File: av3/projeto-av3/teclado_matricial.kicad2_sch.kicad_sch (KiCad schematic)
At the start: 16 parts, among them SW1 SW_Push, SW10 SW_Push, SW11 SW_Push, SW12 SW_Push, SW13 SW_Push, SW14 SW_Push, SW15 SW_Push, SW16 SW_Push, SW2 SW_Push, SW3 SW_Push, SW4 SW_Push, SW5 SW_Push, SW6 SW_Push, SW7 SW_Push, SW8 SW_Push, SW9 SW_Push

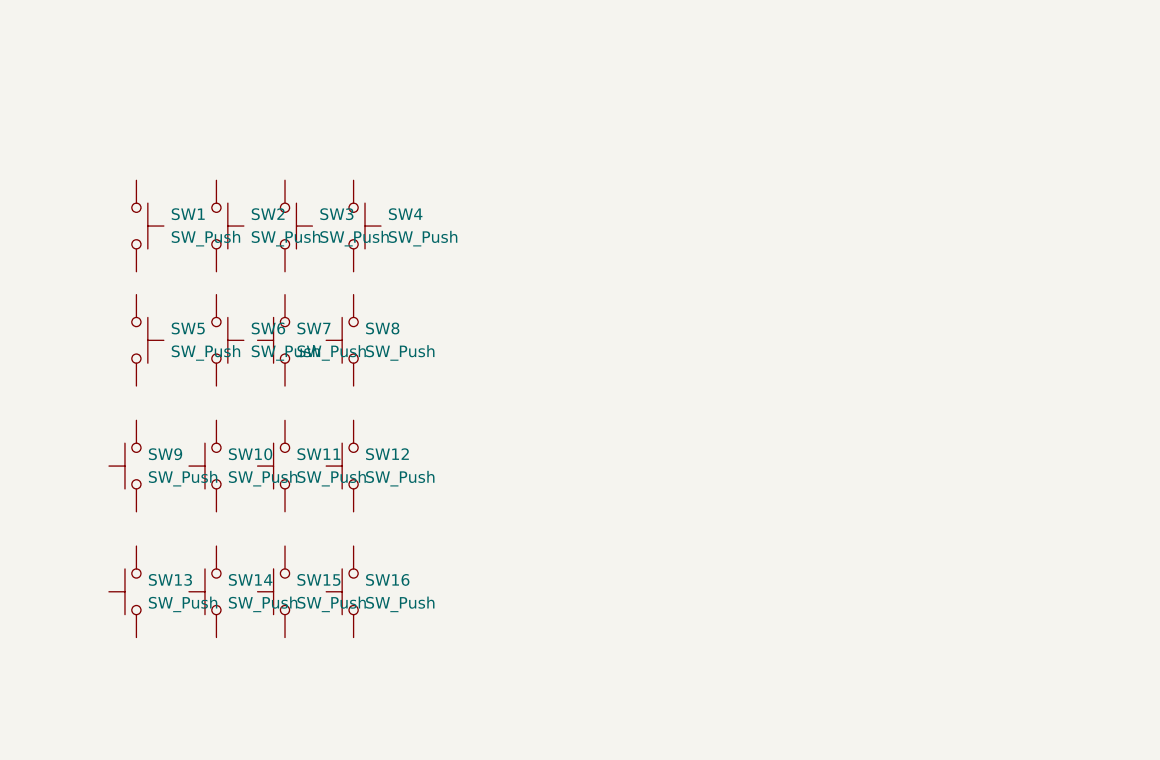
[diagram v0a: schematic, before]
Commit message: Ligação do cristal no atmega2560 e início do esquemático das saídas digitais com relé.
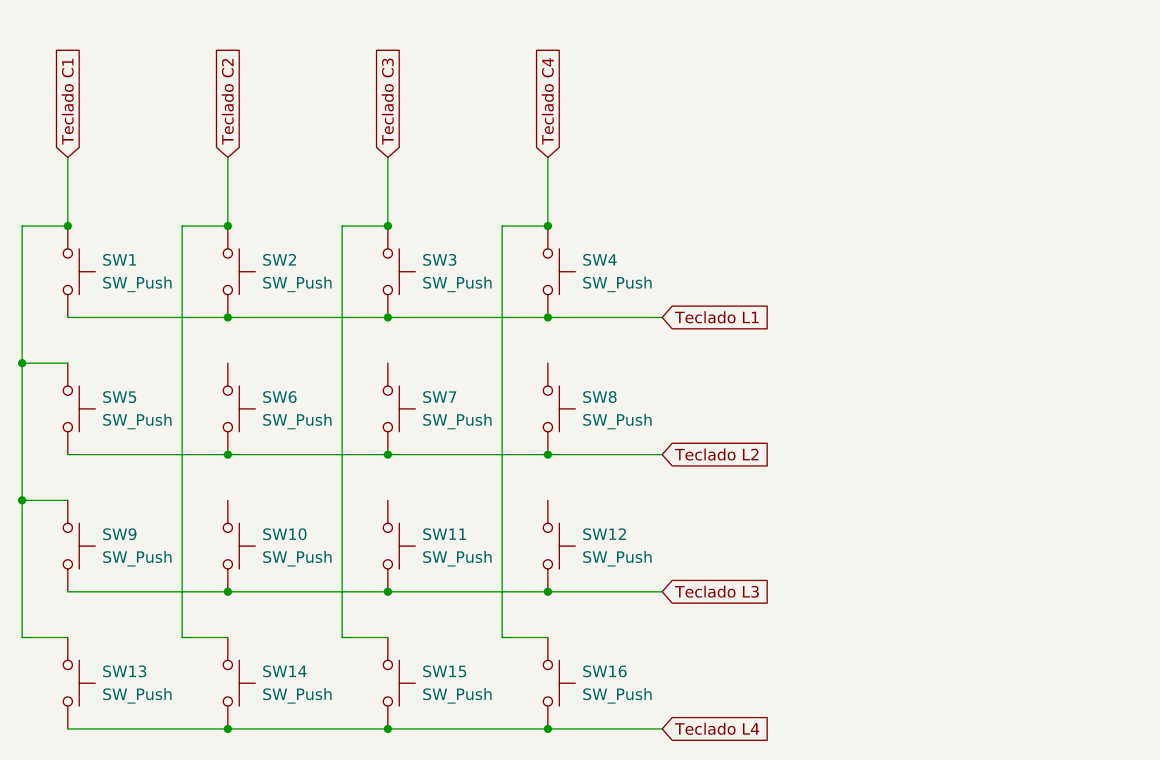
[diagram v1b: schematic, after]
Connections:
- net Teclado L3: now reaches SW10.2
- net Teclado L3: now also SW11.2, SW12.2, SW9.2
- net Teclado L2: now reaches SW7.2
- net Teclado L2: now also SW5.2, SW6.2, SW8.2
- net Teclado C4: now reaches SW16.1
- net Teclado C4: now also SW4.1
- net Teclado L4: now reaches SW16.2
- net Teclado L4: now also SW13.2, SW14.2, SW15.2
- net Teclado L1: now reaches SW4.2
- net Teclado L1: now also SW1.2, SW2.2, SW3.2
- net Teclado C2: now reaches SW2.1
- net Teclado C2: now also SW14.1
- net Teclado C1: now reaches SW1.1
- net Teclado C1: now also SW13.1, SW5.1, SW9.1
- net Teclado C3: now reaches SW15.1
- net Teclado C3: now also SW3.1

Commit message: Maioria dos esquemáticos finalizados.
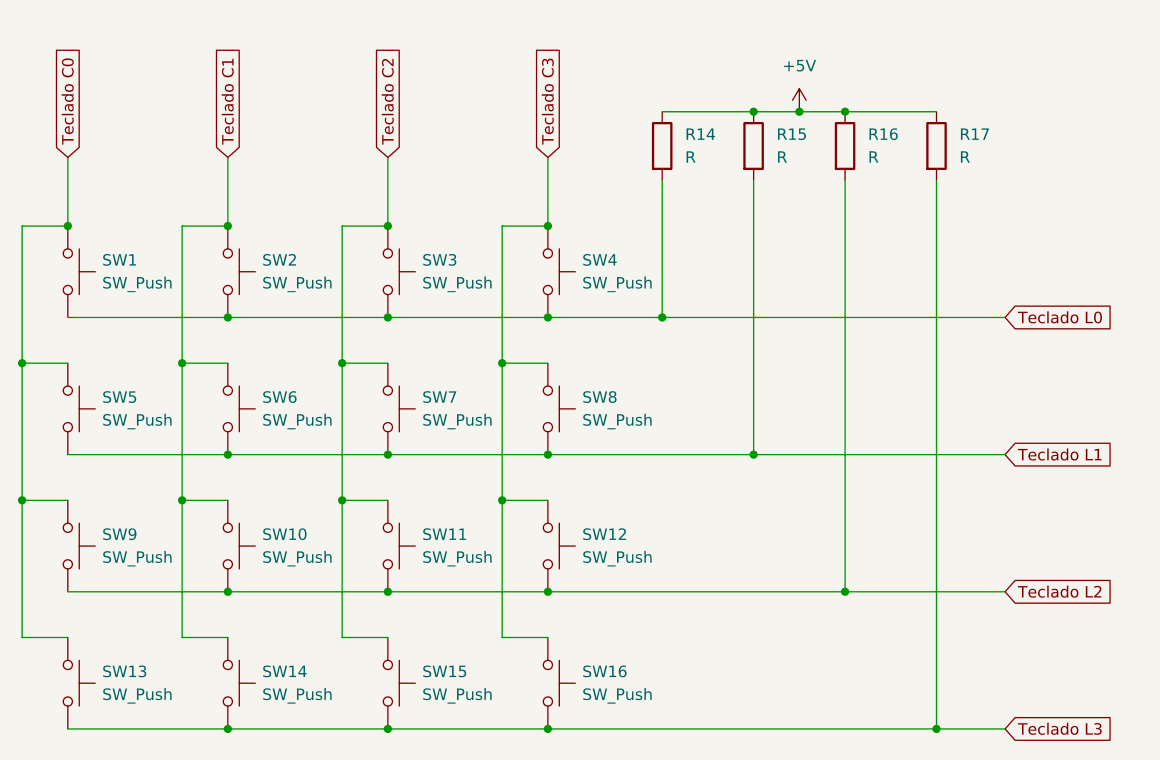
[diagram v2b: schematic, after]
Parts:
- added R14, R15, R16, R17: R, symbol Device:R
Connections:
- net Teclado C4 is gone; now on net Teclado C3: SW16.1, SW4.1
- net Teclado L4 is gone; now on net Teclado L3: SW13.2, SW14.2, SW15.2, SW16.2
- net Teclado C1: now also SW10.1, SW14.1, SW2.1, SW6.1; no longer SW1.1, SW13.1, SW5.1, SW9.1
- net Teclado C2: now also SW11.1, SW15.1, SW3.1, SW7.1; no longer SW14.1, SW2.1
- net Teclado C3: now also SW12.1, SW8.1; no longer SW15.1, SW3.1
- net Teclado L1: now also SW5.2, SW6.2, SW7.2, SW8.2, R15.2; no longer SW1.2, SW2.2, SW3.2, SW4.2
- net Teclado L2: now also SW10.2, SW11.2, SW12.2, SW9.2, R16.2; no longer SW5.2, SW6.2, SW7.2, SW8.2
- net Teclado L3: now also R17.2; no longer SW10.2, SW11.2, SW12.2, SW9.2
- new net +5V: R14.1, R15.1, R16.1, R17.1
- new net Teclado C0: SW1.1, SW13.1, SW5.1, SW9.1
- new net Teclado L0: R14.2, SW1.2, SW2.2, SW3.2, SW4.2

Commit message: Esquemático finalizado, faltando somente o PCB.
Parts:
- R14, R15, R16, R17: value R -> 10k; footprint (none) -> Resistor_SMD:R_1206_3216Metric_Pad1.30x1.75mm_HandSolder
- SW1, SW10, SW11, SW12, SW13, SW14, SW15, SW16, SW2, SW3, SW4, SW5, SW6, SW7, SW8, SW9: footprint (none) -> Button_Switch_THT:SW_PUSH_6mm_H4.3mm
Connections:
- net Teclado C0 renamed C1
- net Teclado C1 renamed C2
- net Teclado C2 renamed C3
- net Teclado C3 renamed C4
- net Teclado L0 renamed L1
- net Teclado L1 renamed L2
- net Teclado L2 renamed L3
- net Teclado L3 renamed L4
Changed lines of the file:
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@@
 		)
 	)
-	(global_label "Teclado C2"
+	(global_label "C3"
 		(shape input)
 		(at 123.19 63.5 90)
@@
 		)
 		(property "Intersheetrefs" "${INTERSHEET_REFS}"
-			(at 123.19 49.8107 90)
-			(effects
-				(font
-					(size 1.27 1.27)
-				)
-				(justify left)
-				(hide yes)
-			)
-		)
-	)
-	(global_label "Teclado C3"
+			(at 123.19 58.0353 90)
+			(effects
+				(font
+					(size 1.27 1.27)
+				)
+				(justify left)
+				(hide yes)
+			)
+		)
+	)
+	(global_label "C4"
 		(shape input)
 		(at 140.97 63.5 90)
@@
 		)
 		(property "Intersheetrefs" "${INTERSHEET_REFS}"
-			(at 140.97 49.8107 90)
-			(effects
-				(font
-					(size 1.27 1.27)
-				)
-				(justify left)
-				(hide yes)
-			)
-		)
-	)
-	(global_label "Teclado C0"
+			(at 140.97 58.0353 90)
+			(effects
+				(font
+					(size 1.27 1.27)
+				)
+				(justify left)
+				(hide yes)
+			)
+		)
+	)
+	(global_label "C1"
 		(shape input)
 		(at 87.63 63.5 90)
@@
 		)
 		(property "Intersheetrefs" "${INTERSHEET_REFS}"
-			(at 87.63 49.8107 90)
-			(effects
-				(font
-					(size 1.27 1.27)
-				)
-				(justify left)
-				(hide yes)
-			)
-		)
-	)
-	(global_label "Teclado L3"
+			(at 87.63 58.0353 90)
+			(effects
+				(font
+					(size 1.27 1.27)
+				)
+				(justify left)
+				(hide yes)
+			)
+		)
+	)
+	(global_label "L4"
 		(shape input)
 		(at 191.77 127 0)
@@
 		)
 		(property "Intersheetrefs" "${INTERSHEET_REFS}"
-			(at 205.2174 127 0)
-			(effects
-				(font
-					(size 1.27 1.27)
-				)
-				(justify left)
-				(hide yes)
-			)
-		)
-	)
-	(global_label "Teclado L2"
+			(at 196.9928 127 0)
+			(effects
+				(font
+					(size 1.27 1.27)
+				)
+				(justify left)
+				(hide yes)
+			)
+		)
+	)
+	(global_label "L3"
 		(shape input)
 		(at 191.77 111.76 0)
@@
 		)
 		(property "Intersheetrefs" "${INTERSHEET_REFS}"
-			(at 205.2174 111.76 0)
-			(effects
-				(font
-					(size 1.27 1.27)
-				)
-				(justify left)
-				(hide yes)
-			)
-		)
-	)
-	(global_label "Teclado L0"
+			(at 196.9928 111.76 0)
+			(effects
+				(font
+					(size 1.27 1.27)
+				)
+				(justify left)
+				(hide yes)
+			)
+		)
+	)
+	(global_label "L1"
 		(shape input)
 		(at 191.77 81.28 0)
@@
 		)
 		(property "Intersheetrefs" "${INTERSHEET_REFS}"
-			(at 205.2174 81.28 0)
-			(effects
-				(font
-					(size 1.27 1.27)
-				)
-				(justify left)
-				(hide yes)
-			)
-		)
-	)
-	(global_label "Teclado C1"
+			(at 196.9928 81.28 0)
+			(effects
+				(font
+					(size 1.27 1.27)
+				)
+				(justify left)
+				(hide yes)
+			)
+		)
+	)
+	(global_label "C2"
 		(shape input)
 		(at 105.41 63.5 90)
@@
 		)
 		(property "Intersheetrefs" "${INTERSHEET_REFS}"
-			(at 105.41 49.8107 90)
-			(effects
-				(font
-					(size 1.27 1.27)
-				)
-				(justify left)
-				(hide yes)
-			)
-		)
-	)
-	(global_label "Teclado L1"
+			(at 105.41 58.0353 90)
+			(effects
+				(font
+					(size 1.27 1.27)
+				)
+				(justify left)
+				(hide yes)
+			)
+		)
+	)
+	(global_label "L2"
 		(shape input)
 		(at 191.77 96.52 0)
@@
 		)
 		(property "Intersheetrefs" "${INTERSHEET_REFS}"
-			(at 205.2174 96.52 0)
+			(at 196.9928 96.52 0)
 			(effects
 				(font
@@
 			)
 		)
-		(property "Footprint" ""
+		(property "Footprint" "Button_Switch_THT:SW_PUSH_6mm_H4.3mm"
 			(at 146.05 121.92 0)
 			(effects
@@
 			)
 		)
-		(property "Value" "R"
+		(property "Value" "10k"
 			(at 156.21 63.4999 0)
 			(effects
@@
 			)
 		)
-		(property "Footprint" ""
+		(property "Footprint" "Resistor_SMD:R_1206_3216Metric_Pad1.30x1.75mm_HandSolder"
 			(at 151.892 62.23 90)
 			(effects
@@
 			)
 		)
-		(property "Footprint" ""
+		(property "Footprint" "Button_Switch_THT:SW_PUSH_6mm_H4.3mm"
 			(at 110.49 106.68 0)
 			(effects
@@
 			)
 		)
-		(property "Footprint" ""
+		(property "Footprint" "Button_Switch_THT:SW_PUSH_6mm_H4.3mm"
 			(at 110.49 91.44 0)
 			(effects
@@
 			)
 		)
-		(property "Footprint" ""
+		(property "Footprint" "Button_Switch_THT:SW_PUSH_6mm_H4.3mm"
 			(at 92.71 76.2 0)
 			(effects
@@
 			)
 		)
-		(property "Value" "R"
+		(property "Value" "10k"
 			(at 166.37 63.4999 0)
 			(effects
@@
 			)
 		)
-		(property "Footprint" ""
+		(property "Footprint" "Resistor_SMD:R_1206_3216Metric_Pad1.30x1.75mm_HandSolder"
 			(at 162.052 62.23 90)
 			(effects
@@
 			)
 		)
-		(property "Footprint" ""
+		(property "Footprint" "Button_Switch_THT:SW_PUSH_6mm_H4.3mm"
 			(at 146.05 91.44 0)
 			(effects
@@
 			)
 		)
-		(property "Value" "R"
+		(property "Value" "10k"
 			(at 186.69 63.4999 0)
 			(effects
@@
 			)
 		)
-		(property "Footprint" ""
+		(property "Footprint" "Resistor_SMD:R_1206_3216Metric_Pad1.30x1.75mm_HandSolder"
 			(at 182.372 62.23 90)
 			(effects
@@
 			)
 		)
-		(property "Footprint" ""
+		(property "Footprint" "Button_Switch_THT:SW_PUSH_6mm_H4.3mm"
 			(at 92.71 106.68 0)
 			(effects
@@
 			)
 		)
-		(property "Footprint" ""
+		(property "Footprint" "Button_Switch_THT:SW_PUSH_6mm_H4.3mm"
 			(at 128.27 121.92 0)
 			(effects
@@
 			)
 		)
-		(property "Footprint" ""
+		(property "Footprint" "Button_Switch_THT:SW_PUSH_6mm_H4.3mm"
 			(at 92.71 91.44 0)
 			(effects
@@
 			)
 		)
-		(property "Footprint" ""
+		(property "Footprint" "Button_Switch_THT:SW_PUSH_6mm_H4.3mm"
 			(at 128.27 106.68 0)
 			(effects
@@
 			)
 		)
-		(property "Footprint" ""
+		(property "Footprint" "Button_Switch_THT:SW_PUSH_6mm_H4.3mm"
 			(at 110.49 76.2 0)
 			(effects
@@
 			)
 		)
-		(property "Footprint" ""
+		(property "Footprint" "Button_Switch_THT:SW_PUSH_6mm_H4.3mm"
 			(at 146.05 106.68 0)
 			(effects
@@
 			)
 		)
-		(property "Footprint" ""
+		(property "Footprint" "Button_Switch_THT:SW_PUSH_6mm_H4.3mm"
 			(at 128.27 76.2 0)
 			(effects
@@
 			)
 		)
-		(property "Value" "R"
+		(property "Value" "10k"
 			(at 176.53 63.4999 0)
 			(effects
@@
 			)
 		)
-		(property "Footprint" ""
+		(property "Footprint" "Resistor_SMD:R_1206_3216Metric_Pad1.30x1.75mm_HandSolder"
 			(at 172.212 62.23 90)
 			(effects
@@
 			)
 		)
-		(property "Footprint" ""
+		(property "Footprint" "Button_Switch_THT:SW_PUSH_6mm_H4.3mm"
 			(at 92.71 121.92 0)
 			(effects
@@
 			)
 		)
-		(property "Footprint" ""
+		(property "Footprint" "Button_Switch_THT:SW_PUSH_6mm_H4.3mm"
 			(at 146.05 76.2 0)
 			(effects
@@
 			)
 		)
-		(property "Footprint" ""
+		(property "Footprint" "Button_Switch_THT:SW_PUSH_6mm_H4.3mm"
 			(at 128.27 91.44 0)
 			(effects
@@
 			)
 		)
-		(property "Footprint" ""
+		(property "Footprint" "Button_Switch_THT:SW_PUSH_6mm_H4.3mm"
 			(at 110.49 121.92 0)
 			(effects

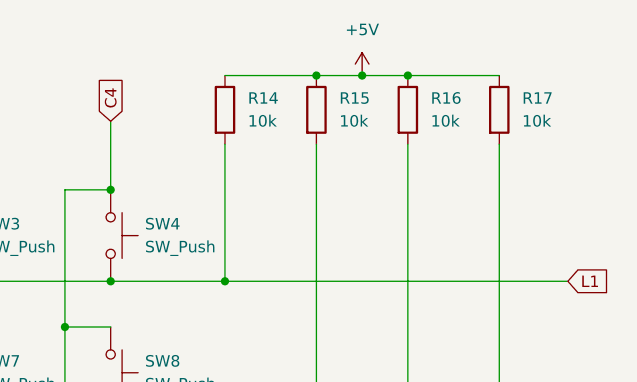
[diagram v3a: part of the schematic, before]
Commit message: Referencias de componentes resetados; Progresso de 20% no PCB;
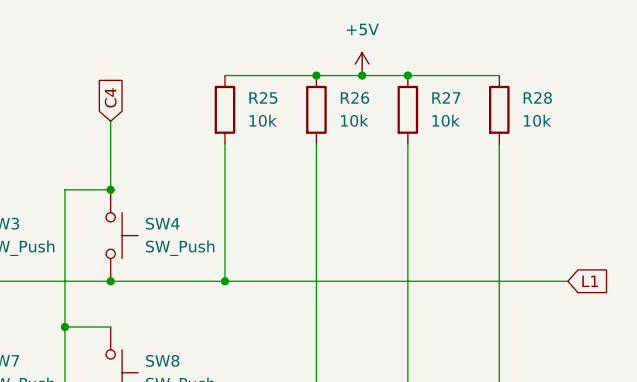
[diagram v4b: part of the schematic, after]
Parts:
- renumbered R14 to R25, R15 to R26, R16 to R27, R17 to R28
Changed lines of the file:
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@@
 		(dnp no)
 		(fields_autoplaced yes)
-		(property "Reference" "R14"
+		(property "Reference" "R25"
 			(at 156.21 60.9599 0)
 			(effects
@@
 			(project "av3"
 				(path "/82998b71-606c-4e03-99b7-477e2a65cb94/93efd14b-15b4-4ad0-945d-8c6626c8e4c1"
-					(reference "R14")
+					(reference "R25")
 					(unit 1)
 				)
@@
 		(dnp no)
 		(fields_autoplaced yes)
-		(property "Reference" "R15"
+		(property "Reference" "R26"
 			(at 166.37 60.9599 0)
 			(effects
@@
 			(project "av3"
 				(path "/82998b71-606c-4e03-99b7-477e2a65cb94/93efd14b-15b4-4ad0-945d-8c6626c8e4c1"
-					(reference "R15")
+					(reference "R26")
 					(unit 1)
 				)
@@
 		(dnp no)
 		(fields_autoplaced yes)
-		(property "Reference" "R17"
+		(property "Reference" "R28"
 			(at 186.69 60.9599 0)
 			(effects
@@
 			(project "av3"
 				(path "/82998b71-606c-4e03-99b7-477e2a65cb94/93efd14b-15b4-4ad0-945d-8c6626c8e4c1"
-					(reference "R17")
+					(reference "R28")
 					(unit 1)
 				)
@@
 		(dnp no)
 		(fields_autoplaced yes)
-		(property "Reference" "R16"
+		(property "Reference" "R27"
 			(at 176.53 60.9599 0)
 			(effects
@@
 			(project "av3"
 				(path "/82998b71-606c-4e03-99b7-477e2a65cb94/93efd14b-15b4-4ad0-945d-8c6626c8e4c1"
-					(reference "R16")
+					(reference "R27")
 					(unit 1)
 				)
@@
 		(dnp no)
 		(fields_autoplaced yes)
-		(property "Reference" "#PWR032"
+		(property "Reference" "#PWR017"
 			(at 168.91 62.23 0)
 			(effects
@@
 			(project "av3"
 				(path "/82998b71-606c-4e03-99b7-477e2a65cb94/93efd14b-15b4-4ad0-945d-8c6626c8e4c1"
-					(reference "#PWR032")
-					(unit 1)
-				)
+					(reference "#PWR017")
+					(unit 1)
+				)
